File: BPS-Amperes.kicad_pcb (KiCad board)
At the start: 2 copper layers, 58.2 x 30.2 mm, 30 parts, among them J1 ShuntConn, J2 LeaderConn, J3 Conn_01x04, U1 AD8417, U2 RO-123.3S_HP, U3 LTC6820, U4 HX1188FNL, U5 ADS7042xDCU

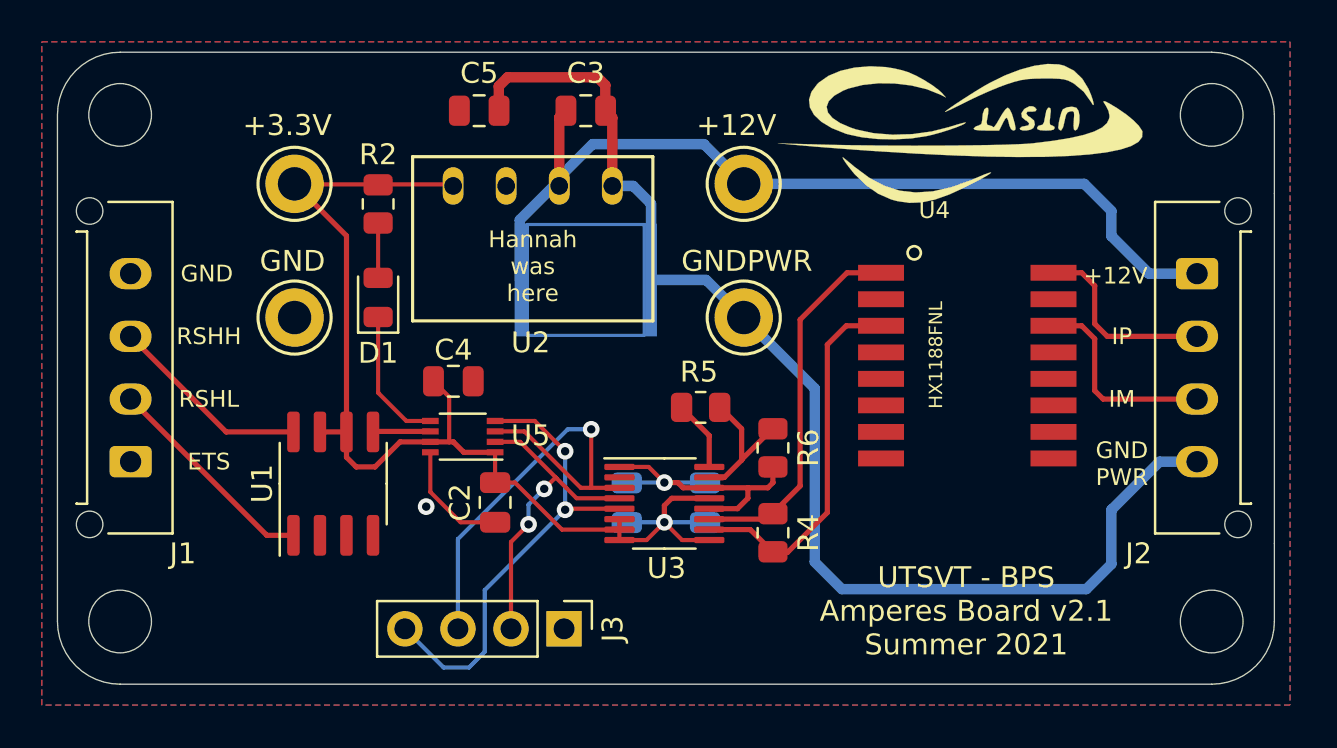
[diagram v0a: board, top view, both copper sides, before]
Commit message: Set up for new amplification scheme
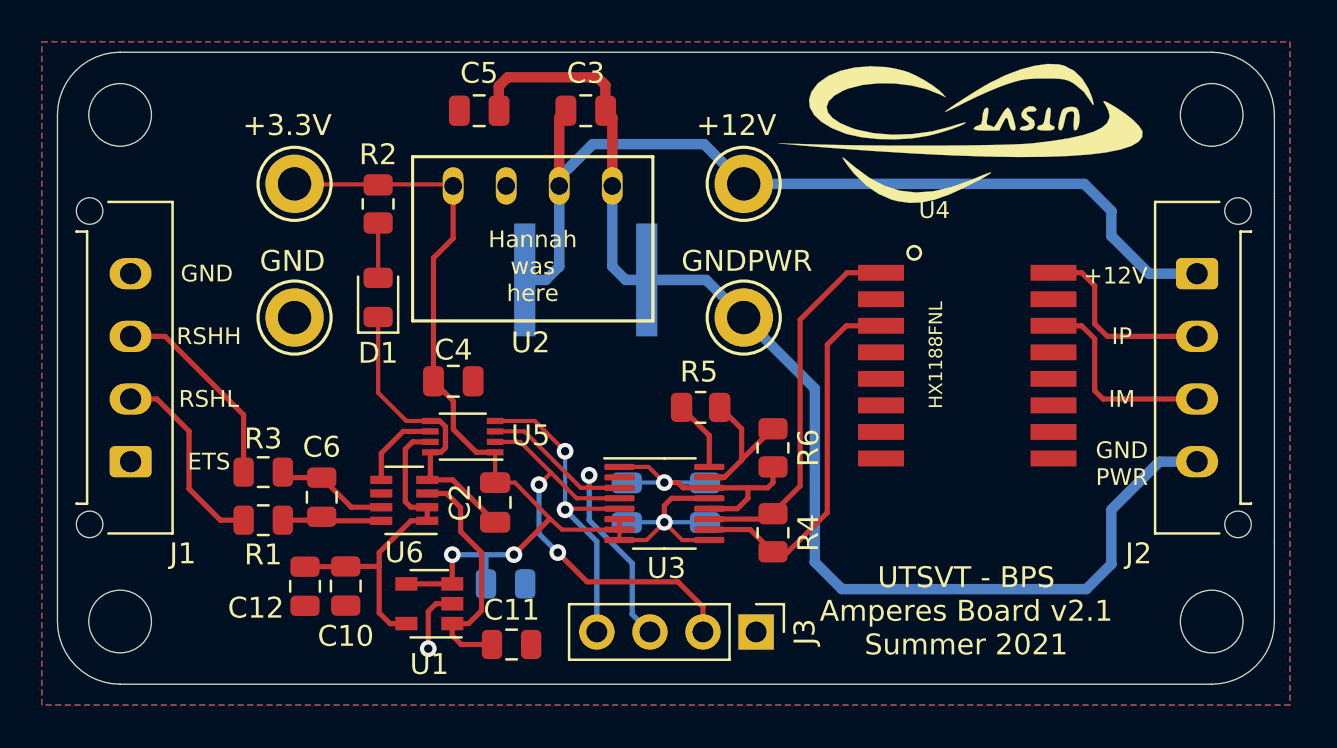
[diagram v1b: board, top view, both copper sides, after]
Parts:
- added C10: 1uF, Capacitor_SMD:C_0805_2012Metric, F.Cu at (101.5, 122.5)
- added C11: 100nF, Capacitor_SMD:C_0805_2012Metric, F.Cu at (109.5, 125.3)
- added C12: 100nF, Capacitor_SMD:C_0805_2012Metric, F.Cu at (99.6, 122.6)
- added C6: 22uF, Capacitor_SMD:C_0805_2012Metric, F.Cu at (100.4, 118.3)
- added C7: 100nF, Capacitor_SMD:C_0805_2012Metric, B.Cu at (109.2, 122.5)
- added R1: 500, Resistor_SMD:R_0805_2012Metric, F.Cu at (97.6, 119.4)
- added R3: 500, Resistor_SMD:R_0805_2012Metric, F.Cu at (97.6, 117.1)
- added U6: INA186A3IDDFT, Package_TO_SOT_SMD:SOT-23-8, F.Cu at (104.3, 118.5)
- U1: value AD8417 -> REF1930AIDDCT; footprint Package_SO:SOIC-8_3.9x4.9mm_P1.27mm -> Package_TO_SOT_SMD:SOT-23-5
- moved J3 9.19 mm to (121.2, 124.8)
- moved U1 7.36 mm to (105.5, 123.4), turned to 180 degrees
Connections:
- J1 pad 2: /RSHL -> Net-(J1-Pad2)
- J1 pad 3: /RSHH -> Net-(J1-Pad3)
- U1 pad 1: /RSHL -> +1V5
- U1 pad 3: GND -> +3V3
- U1 pad 4: (no net) -> +3V3
- U1 pad 5: Net-(U1-Pad5) -> +3V0
- U5 pad 6: Net-(U1-Pad5) -> Net-(U5-Pad6)
- U5 pad 7: +3V3 -> +3V0
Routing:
- net +3V0: track 0.00 -> 16.6 mm
- net +1V5: track 0.00 -> 11.5 mm
- net /RSHL: track 10.5 -> 0.00 mm
- net GND: track 27.2 -> 37.7 mm
- net Net-(J1-Pad3): track 0.00 -> 9.71 mm
- net Net-(J1-Pad2): track 0.00 -> 9.43 mm
- net /CS: track 22.7 -> 15.9 mm
- net /MISO: track 22.7 -> 16.4 mm
- net /SCK: track 15.2 -> 20.7 mm
- net /RSHH: track 9.69 -> 5.41 mm
- net Net-(U5-Pad6): track 0.00 -> 4.05 mm
- net Net-(U1-Pad5): track 2.76 -> 0.00 mm
- net +3V3: track 55.4 -> 54.1 mm, vias 1 -> 3

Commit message: Revised with LTC ADC
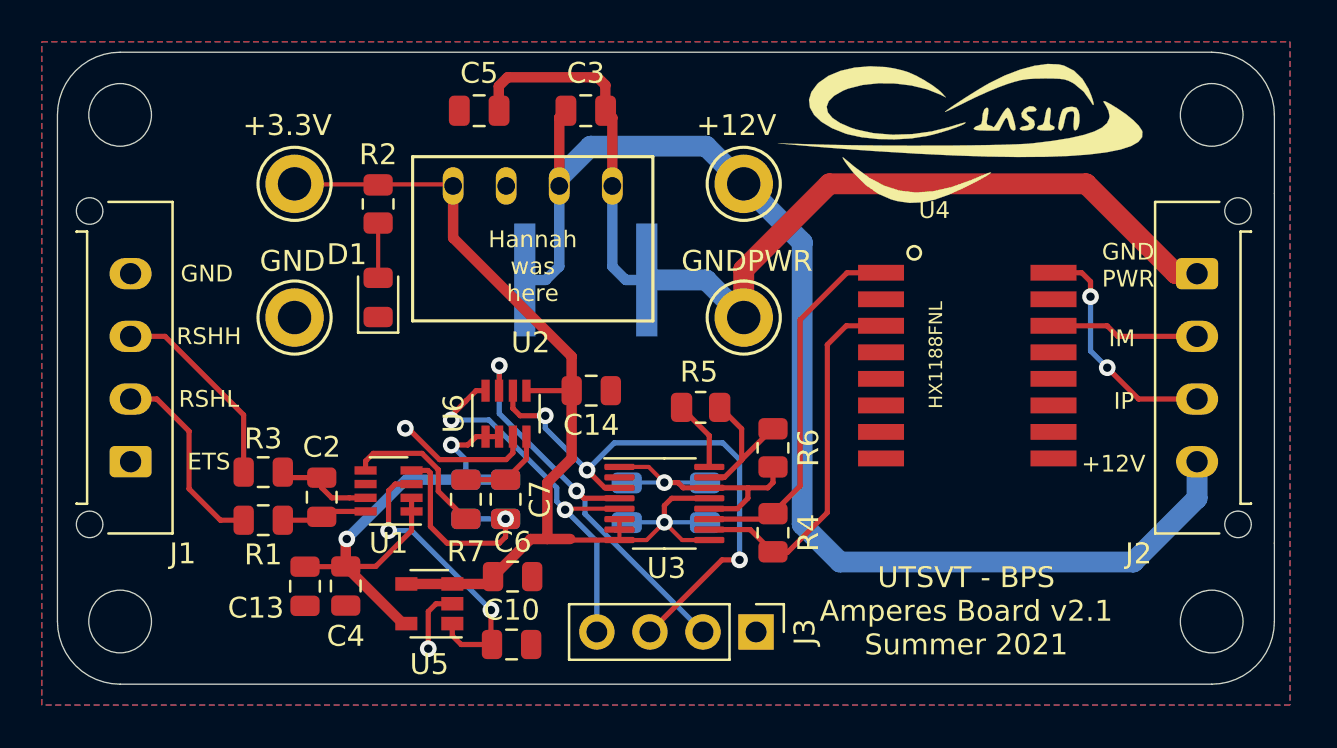
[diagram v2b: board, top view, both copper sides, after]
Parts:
- removed the C2 at (108.7, 118.6)
- removed the C4 at (106.7, 112.8)
- removed the U5 at (107.2, 115.4)
- added C11: 2.2uF, Capacitor_SMD:C_0805_2012Metric, B.Cu at (107.3, 118.4)
- added C12: 2.2uF, Capacitor_SMD:C_0805_2012Metric, B.Cu at (109.2, 118.4)
- added C14: 2.2uF, Capacitor_SMD:C_0805_2012Metric, F.Cu at (113.3, 113.2)
- added C7: 47pF, Capacitor_SMD:C_0805_2012Metric, F.Cu at (109.2, 118.4)
- added R7: 49.9, Resistor_SMD:R_0805_2012Metric, F.Cu at (107.3, 118.4)
- added U6: LTC2315, Package_TO_SOT_SMD:SOT-23-8, F.Cu at (109.2, 114.3)
- C6: renamed from C7; moved to F.Cu
- moved U1 0.87 mm to (103.6, 118.0)
- moved C6 0.49 mm to (109.5, 122.1)
- renumbered C11 to C10, C12 to C13, C6 to C2, C10 to C4, U6 to U1, U1 to U5
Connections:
- J2 pad 1: +12V -> GNDPWR
- J2 pad 4: GNDPWR -> +12V
- U4 pad 14: Net-(J2-Pad3) -> Net-(J2-Pad2)
- U4 pad 16: Net-(J2-Pad2) -> Net-(J2-Pad3)
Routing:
- net +12V: track 44.4 -> 60.2 mm
- net /MISO: track 16.4 -> 26.6 mm, vias 1 -> 3
- net +3V0: track 16.6 -> 25.9 mm, vias 0 -> 2
- net GNDPWR: track 58.5 -> 50.2 mm
- net Net-(C7-Pad1): track 0.00 -> 4.38 mm
- net Net-(R7-Pad2): track 4.05 -> 7.31 mm
- net /CS: track 15.9 -> 19.1 mm
- net +1V5: track 11.5 -> 13.9 mm, vias 0 -> 2
- net Net-(J2-Pad2): track 9.20 -> 7.08 mm
- net Net-(J2-Pad3): track 9.78 -> 11.3 mm, vias 0 -> 2
- net GND: track 37.7 -> 39.2 mm, vias 2 -> 4
- net /RSHH: track 5.41 -> 4.76 mm
- net +3V3: track 54.1 -> 53.5 mm, vias 3 -> 1
- net /SCK: track 20.7 -> 20.2 mm

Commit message: Add additional filtering
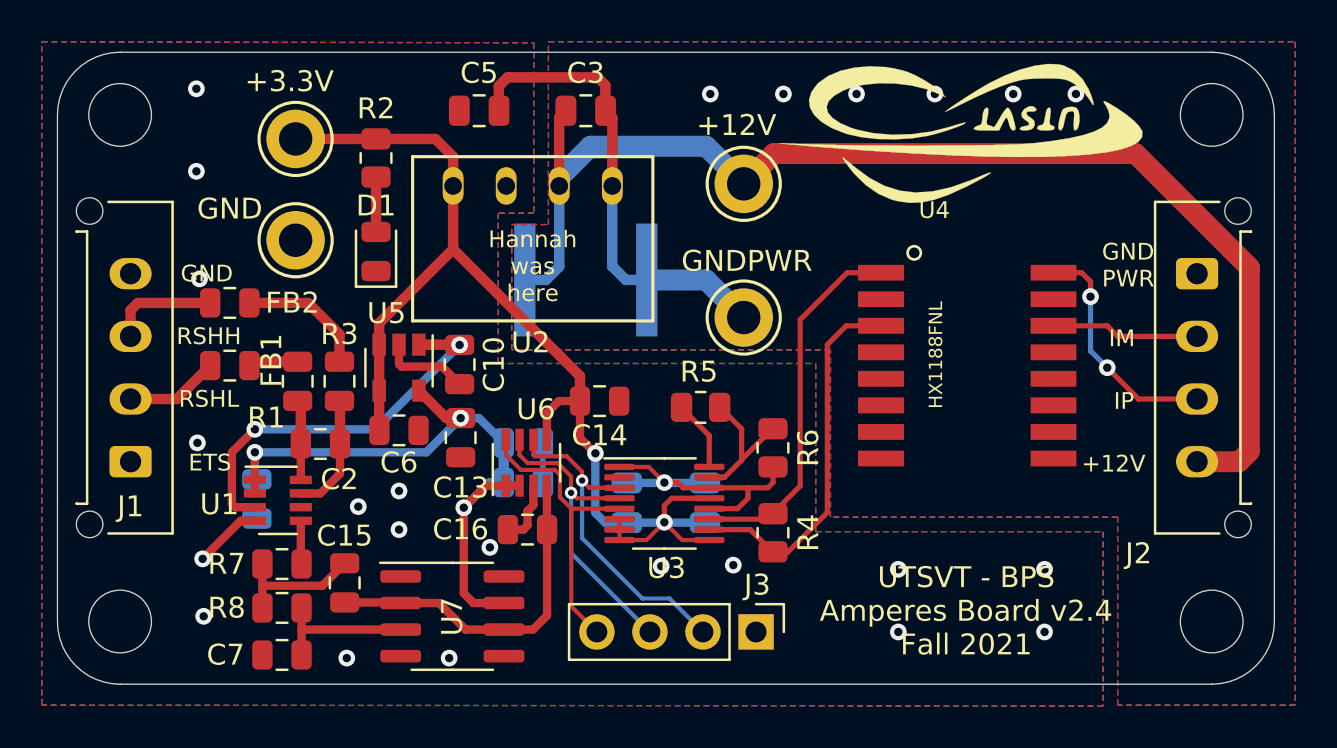
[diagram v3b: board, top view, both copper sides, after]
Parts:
- added C15: 1uF, Capacitor_SMD:C_0805_2012Metric, F.Cu at (101.5, 122.4)
- added C16: 47pF, Capacitor_SMD:C_0805_2012Metric, F.Cu at (110.2, 119.8)
- added FB1: 1.8k, Inductor_SMD:L_0805_2012Metric, F.Cu at (96.0, 112.0)
- added FB2: 1.8k, Inductor_SMD:L_0805_2012Metric, F.Cu at (96.0, 109.0)
- added R8: 10k, Resistor_SMD:R_0805_2012Metric, F.Cu at (98.5, 123.6)
- added U7: OPA192IDR, Package_SO:SOIC-8_3.9x4.9mm_P1.27mm, F.Cu at (106.7, 124.0)
- C4: moved to B.Cu
- C7: value 47pF -> 470nF
- R7: value 49.9 -> 10k
- moved C10 13.6 mm to (107.0, 112.0), turned to 270 degrees
- moved C7 13.0 mm to (98.5, 125.8), turned to 180 degrees
- moved U5 11.4 mm to (104.1, 112.1), turned to 270 degrees
- moved C13 10.3 mm to (107.0, 115.5)
- moved R7 9.33 mm to (98.5, 121.5), turned to 0 degrees
- moved C6 8.86 mm to (104.1, 115.1)
- moved R1 6.85 mm to (99.2, 112.8), turned to 90 degrees
- moved C4 5.95 mm to (97.3, 118.4)
- moved R3 5.68 mm to (101.2, 112.8), turned to 90 degrees
- moved U1 5.32 mm to (98.3, 118.5), turned to 0 degrees
- moved TP4 3.70 mm to (99.2, 106.0)
- moved C11 2.86 mm to (110.0, 117.6), turned to 0 degrees
- moved C12 2.83 mm to (110.0, 115.7), turned to 0 degrees
- moved C2 2.55 mm to (100.3, 115.8), turned to 0 degrees
- moved U6 2.55 mm to (110.2, 116.7)
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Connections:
- C2 pad 1: GND -> /RSHL
- J1 pad 2: Net-(J1-Pad2) -> Net-(FB1-Pad2)
- J1 pad 3: Net-(J1-Pad3) -> Net-(FB2-Pad2)
- J3 pad 2: /SCK -> /MISO
- J3 pad 3: /MISO -> /SCK
- R1 pad 1: GND -> /RSHL
- R1 pad 2: Net-(J1-Pad2) -> Net-(FB1-Pad1)
- R3 pad 2: Net-(J1-Pad3) -> Net-(FB2-Pad1)
- R7 pad 1: Net-(C7-Pad1) -> Net-(C15-Pad2)
- U1 pad 8: GND -> /RSHL
- U6 pad 4: Net-(C7-Pad1) -> Net-(C15-Pad1)
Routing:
- net GNDPWR: track 50.2 -> 22.7 mm, vias 0 -> 6
- net Net-(C15-Pad1): track 0.00 -> 16.7 mm
- net GND: track 39.2 -> 27.4 mm, vias 4 -> 19
- net /MISO: track 26.6 -> 16.2 mm, vias 3 -> 1
- net Net-(J1-Pad3): track 9.71 -> 0.00 mm
- net Net-(J1-Pad2): track 9.43 -> 0.00 mm
- net +3V0: track 25.9 -> 32.6 mm, vias 2 -> 3
- net Net-(C15-Pad2): track 0.00 -> 6.48 mm
- net Net-(FB2-Pad1): track 0.00 -> 6.25 mm
- net Net-(R7-Pad2): track 7.31 -> 2.09 mm
- net Net-(FB2-Pad2): track 0.00 -> 5.21 mm
- net /SCK: track 20.2 -> 15.1 mm, vias 2 -> 1
- net /CS: track 19.1 -> 14.3 mm, vias 2 -> 0
- net +1V5: track 13.9 -> 18.6 mm
- net Net-(FB1-Pad2): track 0.00 -> 4.48 mm
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- added copper zone on B.Cu, net GNDPWR
- added copper zone on F.Cu, net GNDPWR
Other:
- board text added: "UTSVT - BPS Amperes Board v2.4 Fall 2021"
- board text removed: "UTSVT - BPS Amperes Board v2.1 Summer 2021"

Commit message: Add voltage follower before ADC
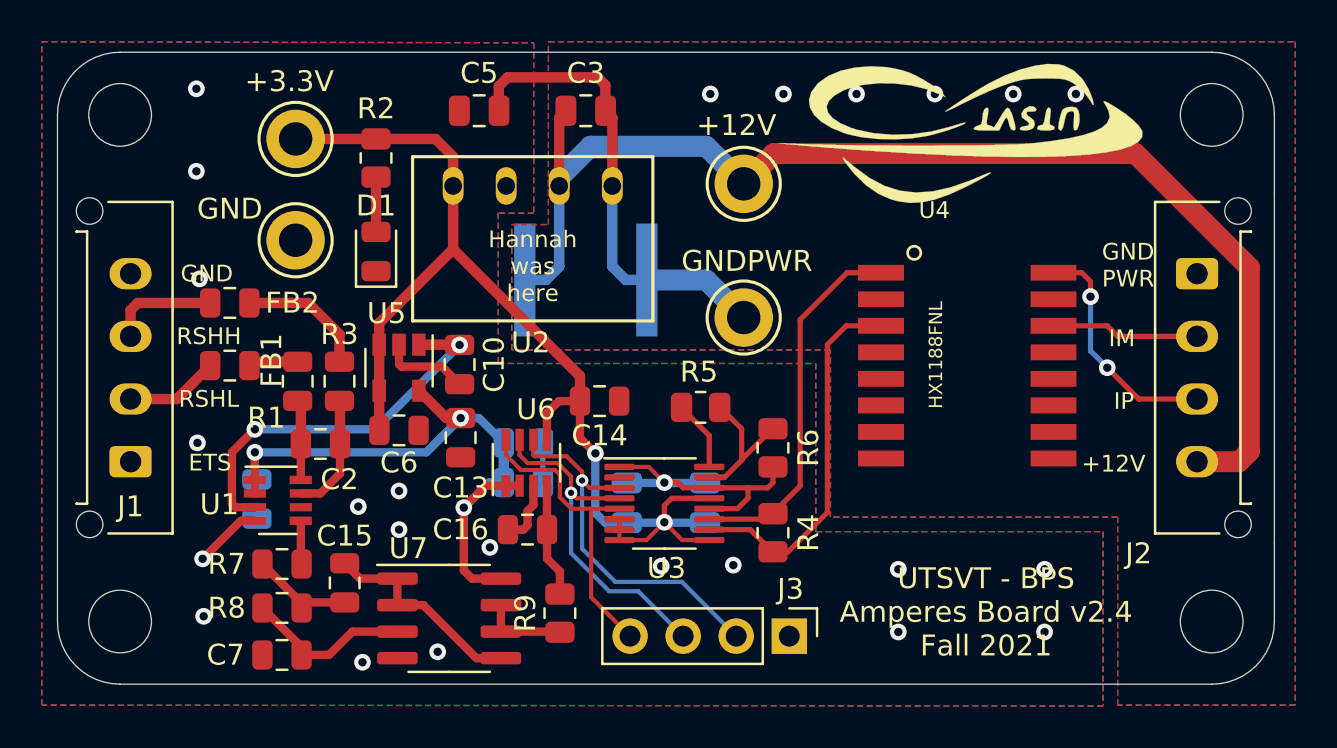
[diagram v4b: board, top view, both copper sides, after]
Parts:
- added R9: 50, Resistor_SMD:R_0805_2012Metric, F.Cu at (111.8, 123.8)
- R1, R3: value 500 -> 1.2k
- U7: value OPA192IDR -> OPA2196
- moved J3 1.60 mm to (122.8, 125.0)
- moved U7 0.18 mm to (106.5, 124.1)
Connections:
- C16 pad 1: Net-(C15-Pad1) -> Net-(C16-Pad1)
- R7 pad 1: Net-(C15-Pad2) -> Net-(C15-Pad1)
- R8 pad 1: Net-(C7-Pad1) -> Net-(C15-Pad1)
- R8 pad 2: Net-(C15-Pad2) -> Net-(C7-Pad1)
- U6 pad 4: Net-(C15-Pad1) -> Net-(C16-Pad1)
- U7 pad 1: (no net) -> Net-(C15-Pad2)
- U7 pad 2: Net-(C15-Pad1) -> Net-(C15-Pad2)
- U7 pad 5: (no net) -> Net-(C15-Pad2)
- U7 pad 6: Net-(C15-Pad1) -> Net-(R9-Pad1)
- U7 pad 7: +3V0 -> Net-(R9-Pad1)
- U7 pad 8: (no net) -> +3V0
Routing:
- net Net-(C15-Pad1): track 16.7 -> 5.03 mm
- net Net-(C16-Pad1): track 0.00 -> 5.44 mm
- net Net-(R9-Pad1): track 0.00 -> 4.11 mm
- net Net-(C15-Pad2): track 6.48 -> 10.1 mm
- net /MISO: track 16.2 -> 18.1 mm
- net /SCK: track 15.1 -> 16.7 mm
- net +3V0: track 32.6 -> 31.3 mm
- net Net-(C7-Pad1): track 6.99 -> 7.91 mm

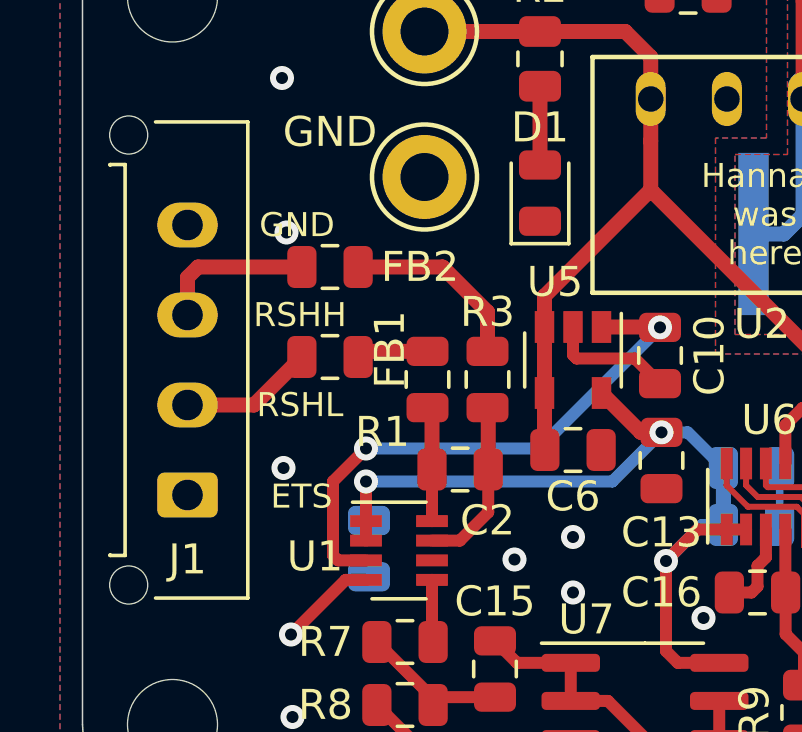
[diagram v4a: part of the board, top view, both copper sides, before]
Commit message: Space out components
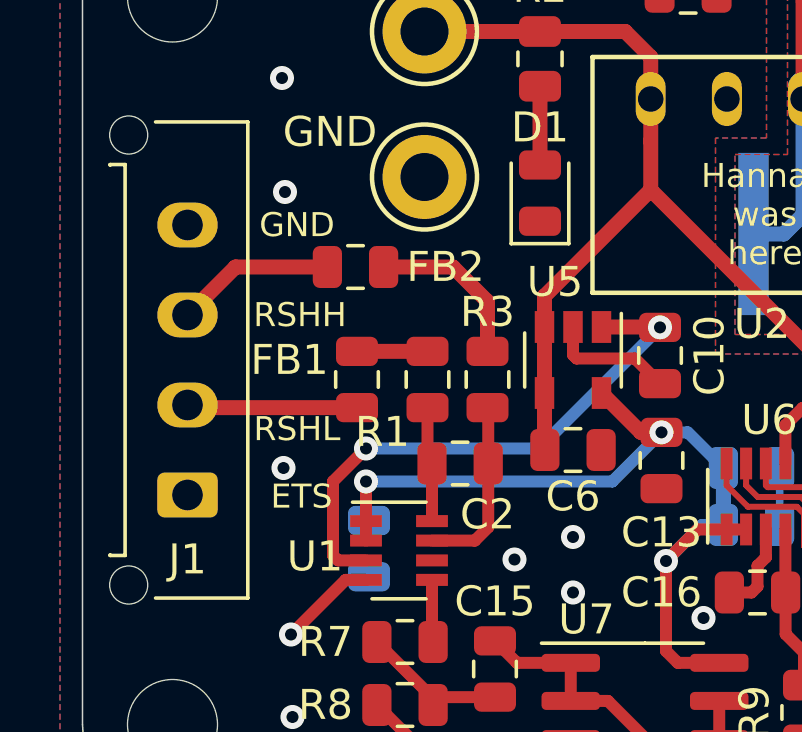
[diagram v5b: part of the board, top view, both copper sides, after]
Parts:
- moved FB1 1.17 mm to (96.9, 112.8), turned to 270 degrees
- moved FB2 0.85 mm to (96.8, 109.0)
- moved C2 0.20 mm to (100.3, 115.5)
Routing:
- net Net-(FB1-Pad2): track 4.48 -> 5.69 mm
- net Net-(FB2-Pad1): track 6.25 -> 5.60 mm

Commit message: Flip logo
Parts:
- turned LOGO2 to 0 degrees

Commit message: Update to what should be the final version
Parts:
- removed D1: PowerOn, LED_SMD:LED_0805_2012Metric
- removed FB1, FB2: 1.8k, Inductor_SMD:L_0805_2012Metric
- C2: value 22uF -> 2.2uF
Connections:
- J1 pad 1: (no net) -> /ETS
- J1 pad 2: Net-(FB1-Pad2) -> GND
- J1 pad 3: Net-(FB2-Pad2) -> Net-(R3-Pad2)
- R1 pad 2: Net-(FB1-Pad1) -> GND
- R2 pad 2: Net-(D1-Pad2) -> unconnected-(R2-Pad2)
- R3 pad 2: Net-(FB2-Pad1) -> Net-(R3-Pad2)
- U1 pad 6: (no net) -> unconnected-(U1-Pad6)
- U3 pad 2: (no net) -> /MOSI
- U4 pad 10: (no net) -> unconnected-(U4-Pad10)
- U4 pad 11: (no net) -> unconnected-(U4-Pad11)
- U4 pad 15: (no net) -> unconnected-(U4-Pad15)
- U4 pad 2: (no net) -> unconnected-(U4-Pad2)
- U4 pad 6: (no net) -> unconnected-(U4-Pad6)
- U4 pad 7: (no net) -> unconnected-(U4-Pad7)
- U4 pad 8: (no net) -> unconnected-(U4-Pad8)
- U4 pad 9: (no net) -> unconnected-(U4-Pad9)
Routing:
- net Net-(R3-Pad2): track 0.00 -> 12.8 mm
- net GND: track 27.4 -> 36.3 mm
- net Net-(FB1-Pad2): track 5.69 -> 0.00 mm
- net Net-(FB2-Pad1): track 5.60 -> 0.00 mm
- net Net-(FB2-Pad2): track 5.33 -> 0.00 mm
- net unconnected-(R2-Pad2): track 0.00 -> 2.62 mm
- net Net-(D1-Pad2): track 2.62 -> 0.00 mm
- net Net-(FB1-Pad1): track 2.35 -> 0.00 mm
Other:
- net class Default removed

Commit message: Minor fixing
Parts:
- added D1: PowerOn, LED_SMD:LED_0805_2012Metric, F.Cu at (103.0, 105.9)
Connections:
- R2 pad 2: unconnected-(R2-Pad2) -> Net-(R2-Pad2)
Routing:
- net unconnected-(R2-Pad2): track 2.62 -> 0.00 mm
- net Net-(R2-Pad2): track 0.00 -> 1.99 mm
- net GND: track 36.3 -> 34.4 mm
